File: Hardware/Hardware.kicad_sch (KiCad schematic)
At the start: 24 parts, among them J1 Conn_01x04, SW1 SW_Push, U1 STM32WB55RGVx, Y1 32kHz768, Y2 32MHz

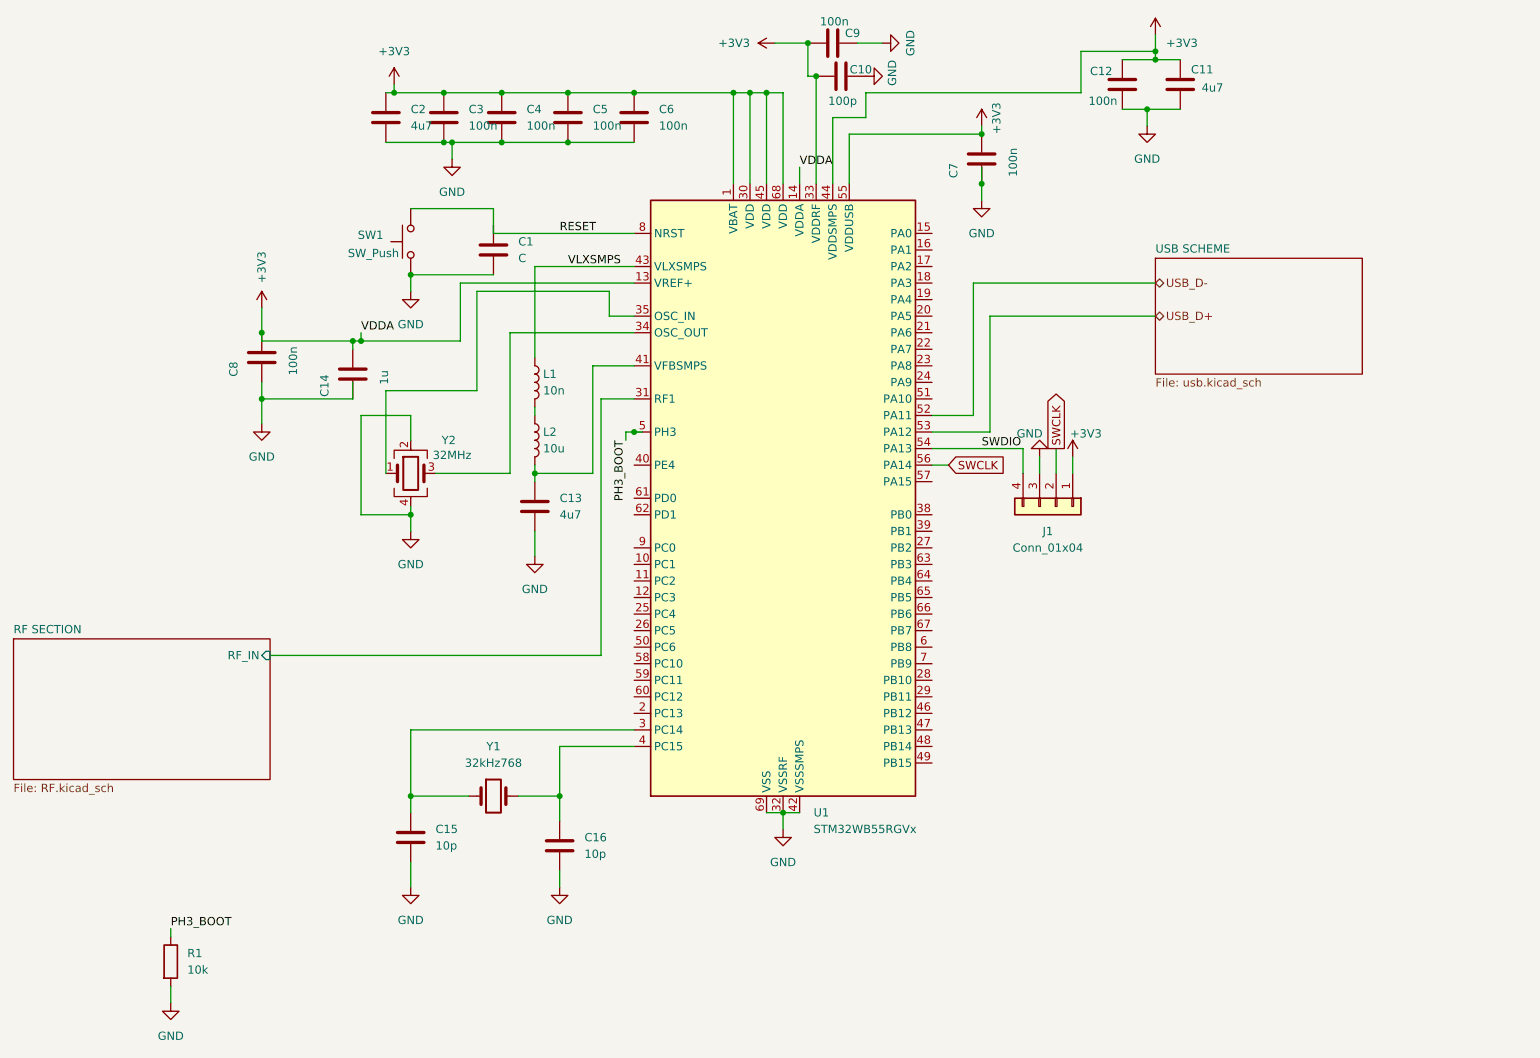
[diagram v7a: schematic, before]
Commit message: [Realisation] : Regulateur de Tension, Capteur BME280, Buzzer, MQ2 et Leds indicateurs.
Dans cette phase, j'ai réalisé les montages suivantes ;
Regulateur de Tension : La tension d'alimentation du système vient de
l'USB, donc en utilisant un regulateur de tension, on parvient à
abaisser la tension à 3.3V
Capteur BME280 : Le montage est réalisé comme recommandé par le
fabricant Bosch. En y précisant les résistance pull up pour le protocol
I2C.
Buzzer : Le buzzer va servir d'alerte en raisonnant.
Pour ce montage on utilise un transistor NPN pour amplifier le courant.
MQ2 : Pour ce capteur, on utilise des éléments traversant et de ce fait,
on va juste souder le composant à la carte.
Led Indicateurs : ces indicateurs vont servir de visuel pour juger le
niveau de la temperature.
D1 : Pour indiquer que la carte est sous tension
D2 : Pour indiquer que la temperature est < 20°C
D3 : Pour indiquer que la temperature est > 20°C et < 30°C
D4 : Pour indiquer que la temperature est > 30°C
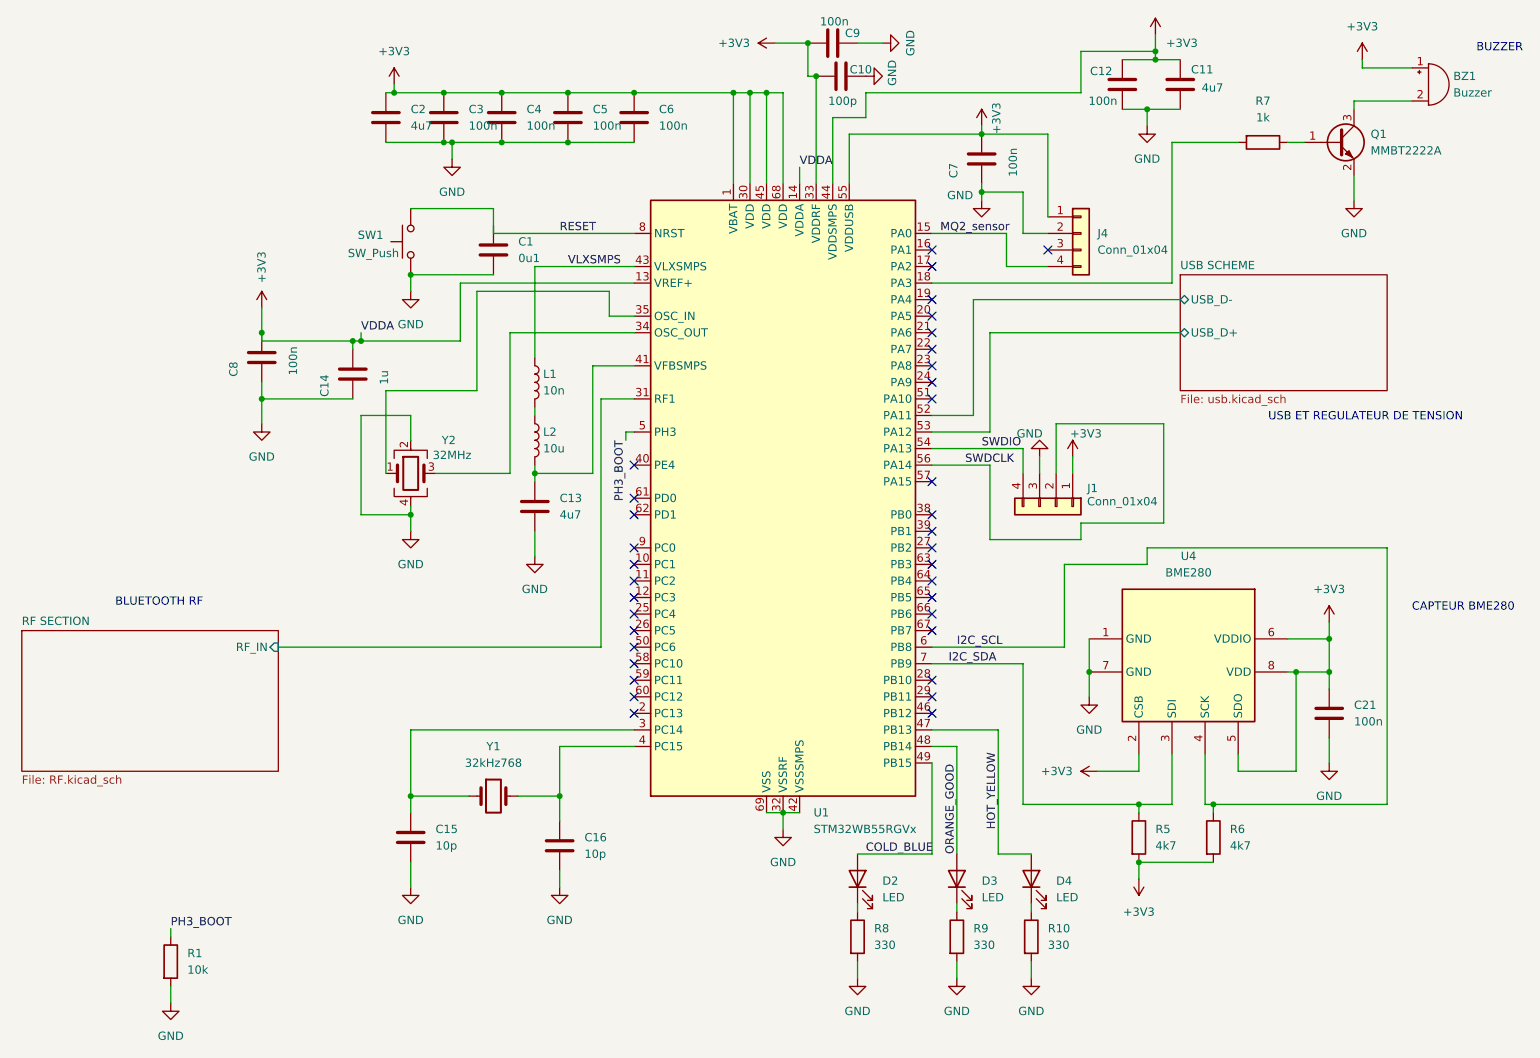
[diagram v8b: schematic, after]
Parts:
- added BZ1: Buzzer, symbol Device:Buzzer
- added C21: 100n, symbol Device:C
- added D2, D3, D4: LED, symbol Device:LED
- added J4: Conn_01x04, symbol Connector_Generic:Conn_01x04
- added Q1: MMBT2222A, Package_TO_SOT_SMD:SOT-23, symbol Transistor_BJT:MMBT2222A
- added R10, R8, R9: 330, symbol Device:R
- added R5, R6: 4k7, symbol Device:R
- added R7: 1k, symbol Device:R
- added U4: BME280, Package_LGA:Bosch_LGA-8_2.5x2.5mm_P0.65mm_ClockwisePinNumbering, symbol Sensor:BME280
- C1: value C -> 0u1
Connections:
- net +3V3: now also BZ1.1 (+), C21.1, J4.1 (Pin_1), R5.2, R6.2, U4.2 (CSB), U4.5 (SDO), U4.6 (VDDIO), U4.8 (VDD)
- net GND: now also C21.2, J4.2 (Pin_2), Q1.2 (E), R10.2, R8.2, R9.2, U4.1 (GND), U4.7 (GND)
- net MQ2_sensor: now reaches U1.15 (PA0)
- net MQ2_sensor: now also J4.4 (Pin_4)
- net at U1.18 (PA3): now also R7.2
- net HOT_YELLOW: now reaches U1.47 (PB13)
- net HOT_YELLOW: now also D4.2 (A)
- net ORANGE_GOOD: now reaches U1.48 (PB14)
- net ORANGE_GOOD: now also D3.2 (A)
- net COLD_BLUE: now reaches U1.49 (PB15)
- net COLD_BLUE: now also D2.2 (A)
- net I2C_SCL: now reaches U1.6 (PB8)
- net I2C_SCL: now also R6.1, U4.4 (SCK)
- net I2C_SDA: now reaches U1.7 (PB9)
- net I2C_SDA: now also R5.1, U4.3 (SDI)
- net SWCLK renamed SWDCLK
- net USB_D+ renamed USB SCHEME/USB_D+
- net USB_D- renamed USB SCHEME/USB_D-
- new net: D4.1 (K), R10.1
- new net: D2.1 (K), R8.1
- new net: D3.1 (K), R9.1
- new net: BZ1.2 (-), Q1.3 (C)
- new net: Q1.1 (B), R7.1
- no-connect marks 0 -> 36
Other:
- sheet USB SCHEME ports: added USB_D+, USB_D-; removed none
- note added: "BLUETOOTH RF"
- note added: "BUZZER"
- note added: "CAPTEUR BME280"
- note added: "USB ET REGULATEUR DE TENSION"
